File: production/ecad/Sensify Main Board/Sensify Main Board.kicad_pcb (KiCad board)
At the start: 4 copper layers, 150 parts, among them J1 1-2834011-3, J2 1-2834011-2, J3 1332645, J4 0532611271, J5 Screw_Terminal_01x08, J6 Conn_01x02_Socket, J7 Conn_01x02_Socket, J8 Conn_01x02_Socket, J9 Conn_01x02_Socket, Q1 2N700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

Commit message: continuing layout for main board
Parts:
- moved R1 220.4 mm to (210.3, 136.3), turned to -90 degrees
- moved R6 218.2 mm to (227.7, 118.3)
- moved R8 210.2 mm to (214.3, 128.5), turned to 180 degrees
- moved R9 209.9 mm to (217.3, 124.4), turned to 180 degrees
- moved R5 204.0 mm to (200.4, 124.4), turned to -90 degrees
- moved C7 200.9 mm to (214.9, 131.8), turned to 90 degrees
- moved R7 198.1 mm to (212.2, 112.5)
- moved BAT1+_TP1 125.7 mm to (112.1, 115.9)
- moved BAT1-/BAT2+_TP1 125.7 mm to (112.1, 119.5)
- moved BAT2-_TP1 125.7 mm to (112.1, 123.0)
- moved BMS_ALERT_TP1 125.7 mm to (112.1, 126.6)
- moved C16 125.7 mm to (96.6, 102.8)
- moved C17 125.7 mm to (101.9, 122.5)
- moved C18 125.7 mm to (96.6, 105.3)
- moved C20 125.7 mm to (96.6, 107.8)
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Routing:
- net (no net): vias 2 -> 0

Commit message: continued main board layout
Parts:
- U5: moved to B.Cu
- moved J3 247.1 mm to (246.7, 108.0)
- moved R31 227.2 mm to (253.1, 96.9), turned to -90 degrees
- moved R29 226.2 mm to (251.8, 96.9), turned to 90 degrees
- moved R28 225.0 mm to (250.6, 96.9), turned to 90 degrees
- moved R30 223.5 mm to (249.3, 96.9), turned to -90 degrees
- moved R25 181.6 mm to (207.8, 66.9)
- moved R32 181.6 mm to (210.7, 66.9)
- moved U6 179.4 mm to (196.6, 108.9)
- moved C24 176.2 mm to (213.2, 46.2)
- moved C25 176.2 mm to (213.2, 48.1)
- moved C26 176.2 mm to (213.2, 50.1)
- moved C27 176.2 mm to (213.2, 52.1)
- moved Q5 176.2 mm to (211.9, 32.4)
- moved Q6 176.2 mm to (211.9, 37.1)
- moved R26 176.2 mm to (200.4, 48.2)
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
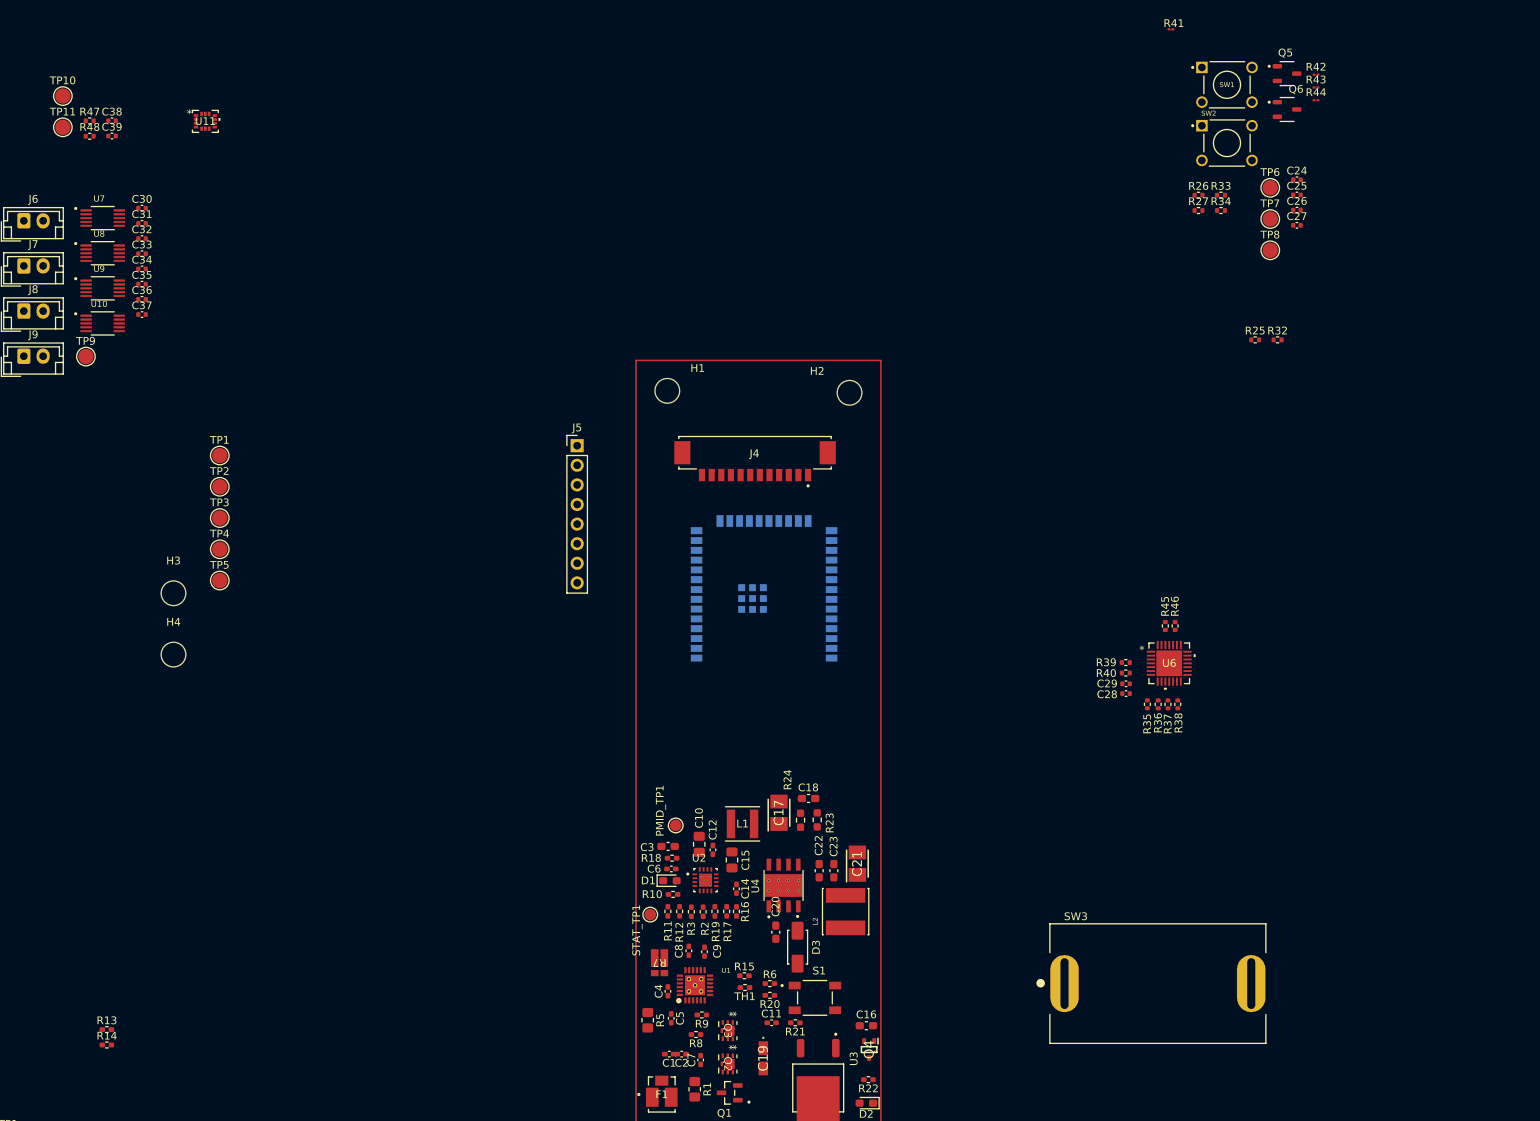
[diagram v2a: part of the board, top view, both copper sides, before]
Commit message: main board layout
rerouted the 5V buck supply according to TI guidelines
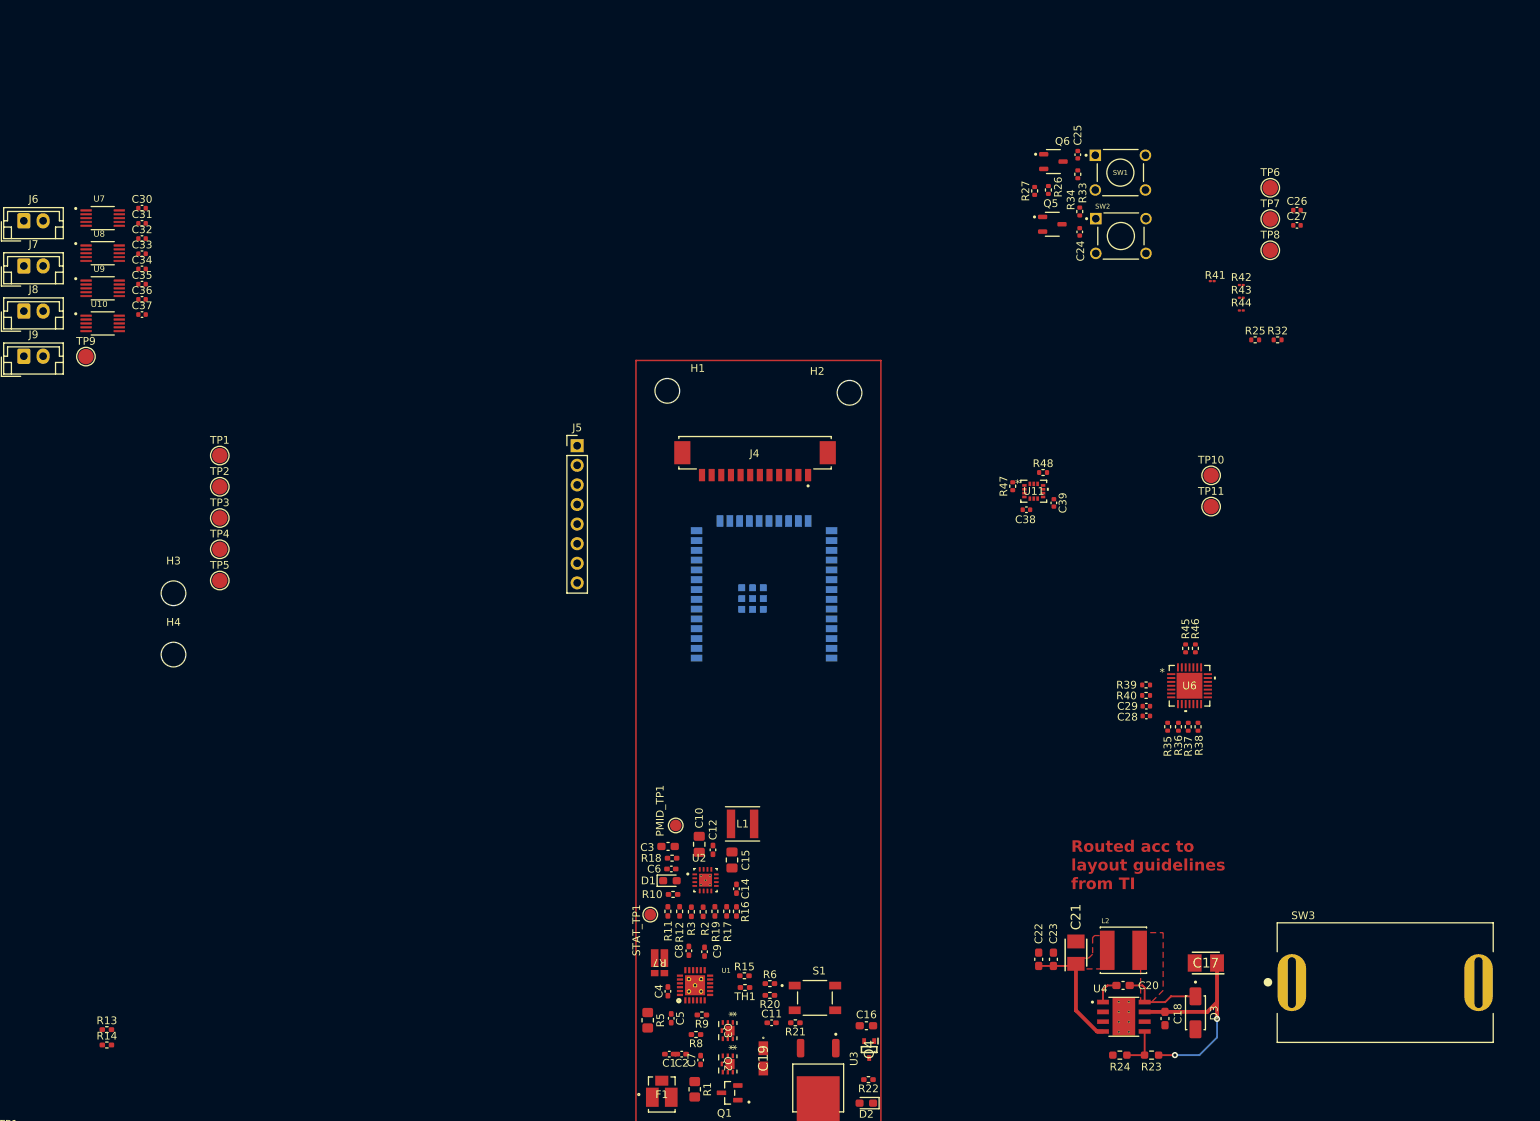
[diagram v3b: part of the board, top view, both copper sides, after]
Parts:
- moved TP10 156.7 mm to (202.1, 84.5)
- moved TP11 156.7 mm to (202.1, 88.5)
- moved R48 131.0 mm to (180.3, 84.1)
- moved C39 131.0 mm to (181.7, 88.1), turned to -90 degrees
- moved C38 128.8 mm to (178.1, 88.9)
- moved R47 128.7 mm to (176.3, 85.9), turned to 90 degrees
- moved U11 117.6 mm to (179.1, 86.5)
- moved C17 58.7 mm to (201.4, 147.7), turned to 180 degrees
- moved C18 54.3 mm to (196.1, 154.9), turned to -90 degrees
- moved R23 53.0 mm to (194.3, 159.6), turned to 180 degrees
- moved D3 52.3 mm to (200.0, 154.2)
- moved R24 51.4 mm to (190.2, 159.6), turned to 180 degrees
- moved U4 47.3 mm to (190.7, 154.7), turned to 0 degrees
- moved C20 45.5 mm to (190.6, 150.6), turned to 0 degrees
- moved L2 36.4 mm to (190.7, 146.1), turned to 180 degrees
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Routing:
- net Net-(SW3-B): track 0.00 -> 28.2 mm, vias 0 -> 2
- net +5V: track 0.00 -> 15.6 mm
- net Net-(U4-SW): track 0.00 -> 10.8 mm
- net Net-(U4-EN): track 0.00 -> 5.41 mm
- net Net-(U4-BOOT): track 0.00 -> 3.56 mm
- added copper zone on F.Cu, net +5V
- added copper zone on F.Cu, net Net-(U4-SW)
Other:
- board text added: "Routed acc to layout guidelines from TI"

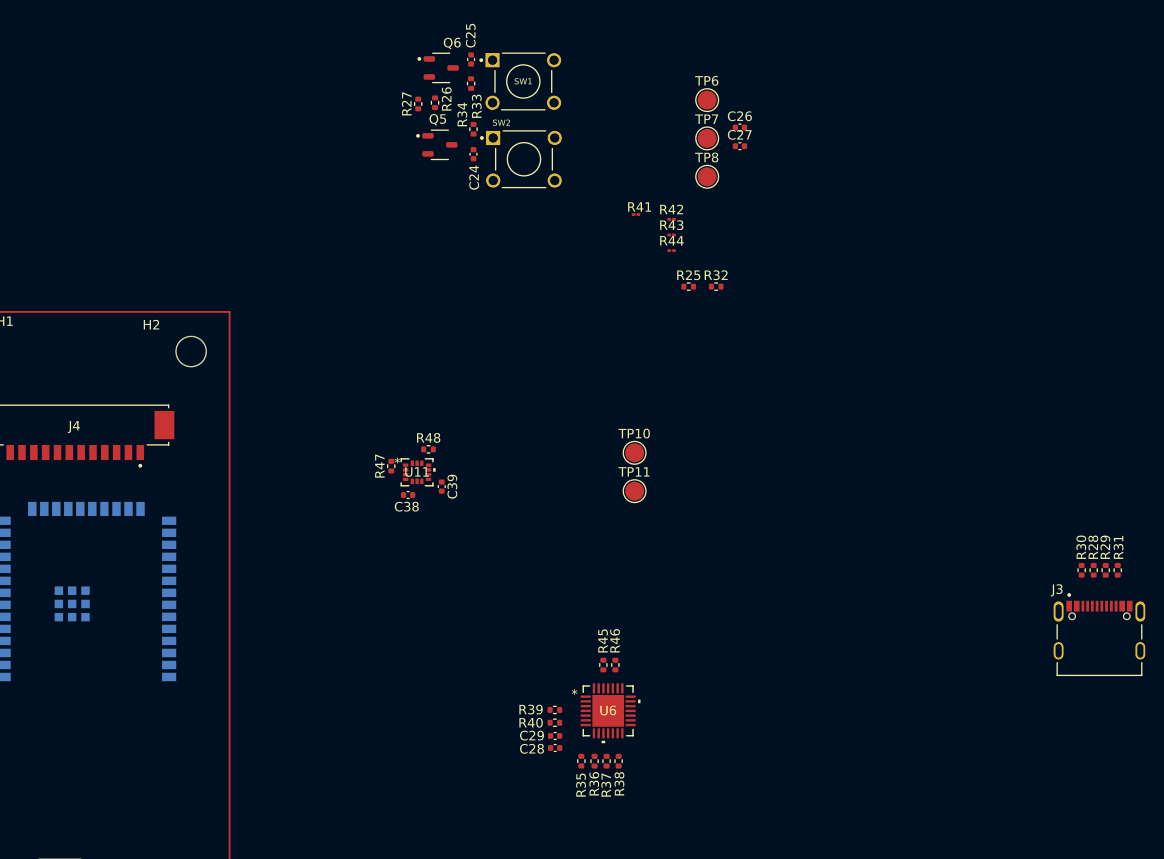
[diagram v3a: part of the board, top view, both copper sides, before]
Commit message: Routed most of USB-UART
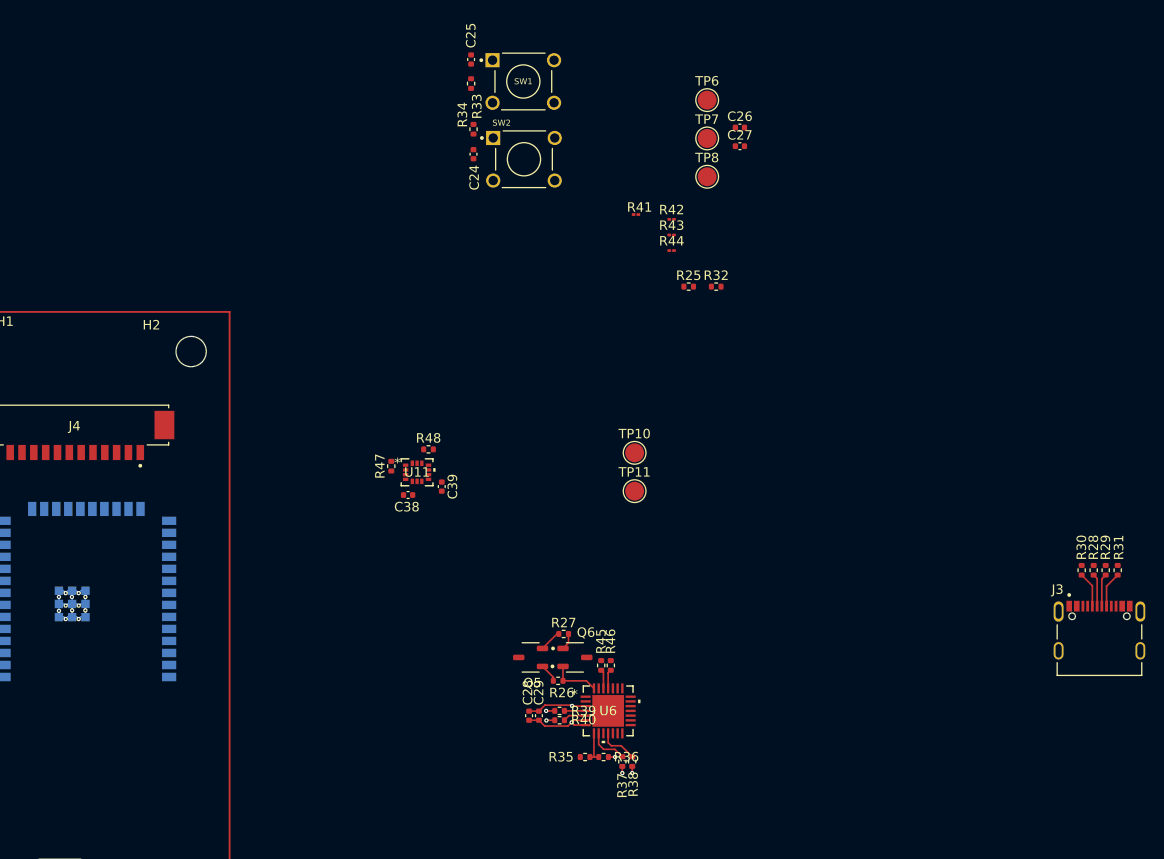
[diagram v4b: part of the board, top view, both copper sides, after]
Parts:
- moved Q6 63.9 mm to (195.7, 106.1)
- moved R26 62.5 mm to (194.0, 108.6), turned to 180 degrees
- moved R27 58.1 mm to (194.6, 103.6), turned to 0 degrees
- moved Q5 55.0 mm to (191.1, 106.1), turned to 180 degrees
- moved C28 4.39 mm to (190.9, 112.3), turned to 90 degrees
- moved C29 2.75 mm to (191.9, 112.3), turned to 90 degrees
- moved R37 1.66 mm to (200.8, 117.1)
- moved R38 1.44 mm to (201.8, 117.1)
- moved R36 1.05 mm to (198.8, 116.6), turned to 0 degrees
- moved R35 0.59 mm to (196.8, 116.6), turned to 0 degrees
- moved R40 0.56 mm to (194.1, 112.8), turned to 180 degrees
- moved R39 0.51 mm to (194.1, 111.8), turned to 180 degrees
- moved R46 0.48 mm to (199.5, 107.0)
- moved R45 0.23 mm to (198.5, 107.0)
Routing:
- net GND: track 0.00 -> 25.7 mm, vias 0 -> 15
- net +3V3: track 0.00 -> 8.80 mm, vias 0 -> 2
- net DTR: track 0.00 -> 5.13 mm
- net Net-(U6-RSTb): track 0.00 -> 4.21 mm
- net Net-(U6-SUSPENDb): track 0.00 -> 4.14 mm
- net Net-(J3-DP2): track 0.00 -> 3.77 mm
- net Net-(J3-DN2): track 0.00 -> 3.75 mm
- net Net-(J3-DN1): track 0.00 -> 3.45 mm
- net Net-(U6-VBUS): track 0.00 -> 3.45 mm
- net Net-(J3-DP1): track 0.00 -> 3.43 mm
- net Net-(U6-D-): track 0.00 -> 2.45 mm
- net RTS: track 0.00 -> 2.36 mm
- net Net-(U6-D+): track 0.00 -> 2.25 mm
- net Net-(U6-TXD): track 0.00 -> 2.17 mm
- net Net-(U6-RXD): track 0.00 -> 2.03 mm
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
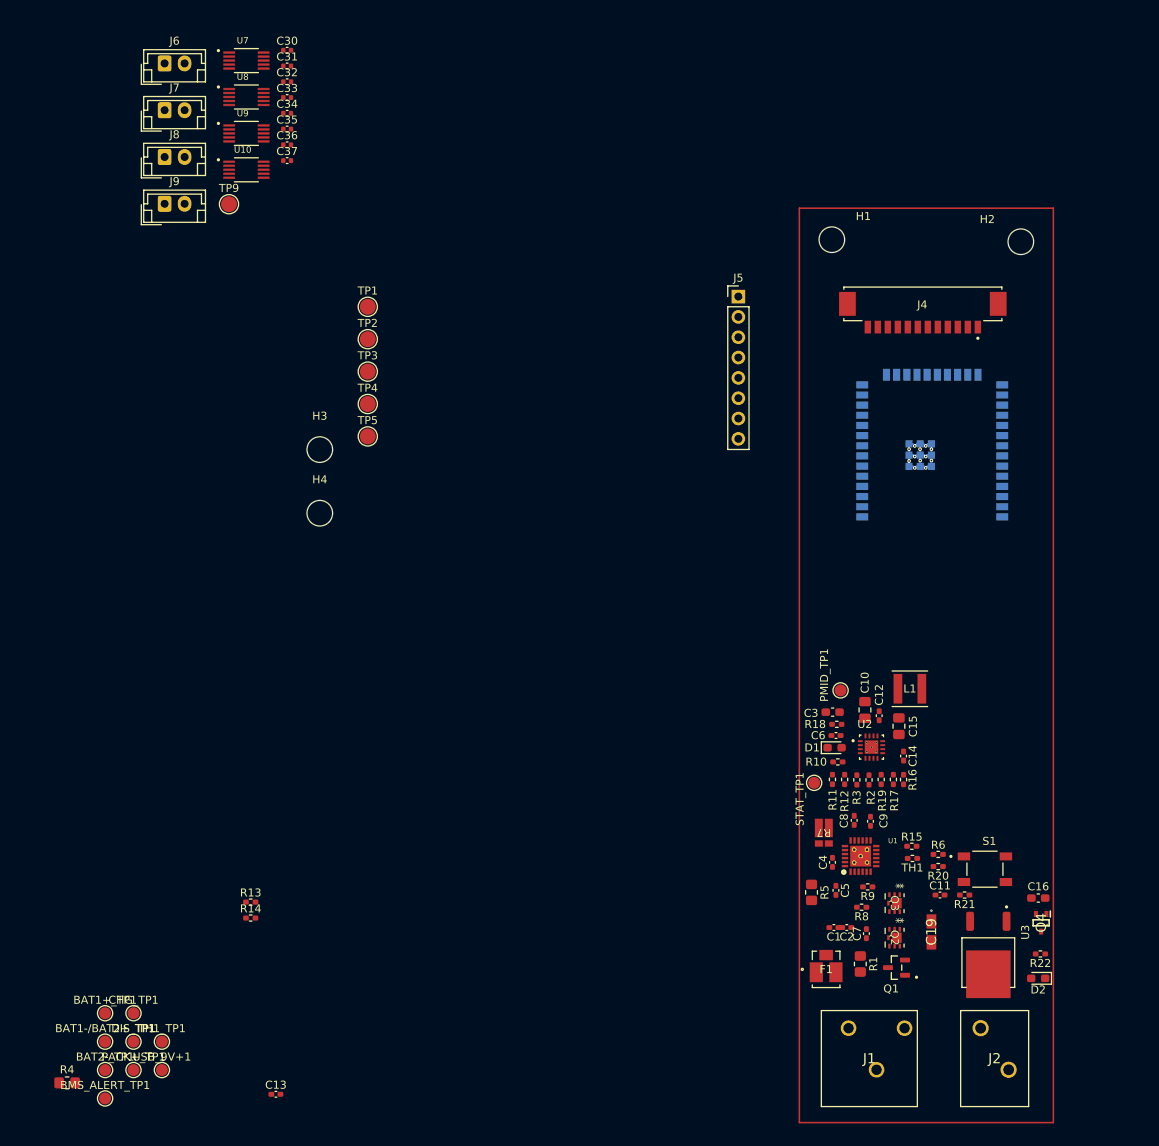
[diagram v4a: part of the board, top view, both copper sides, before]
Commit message: placed BMS components minus TPs
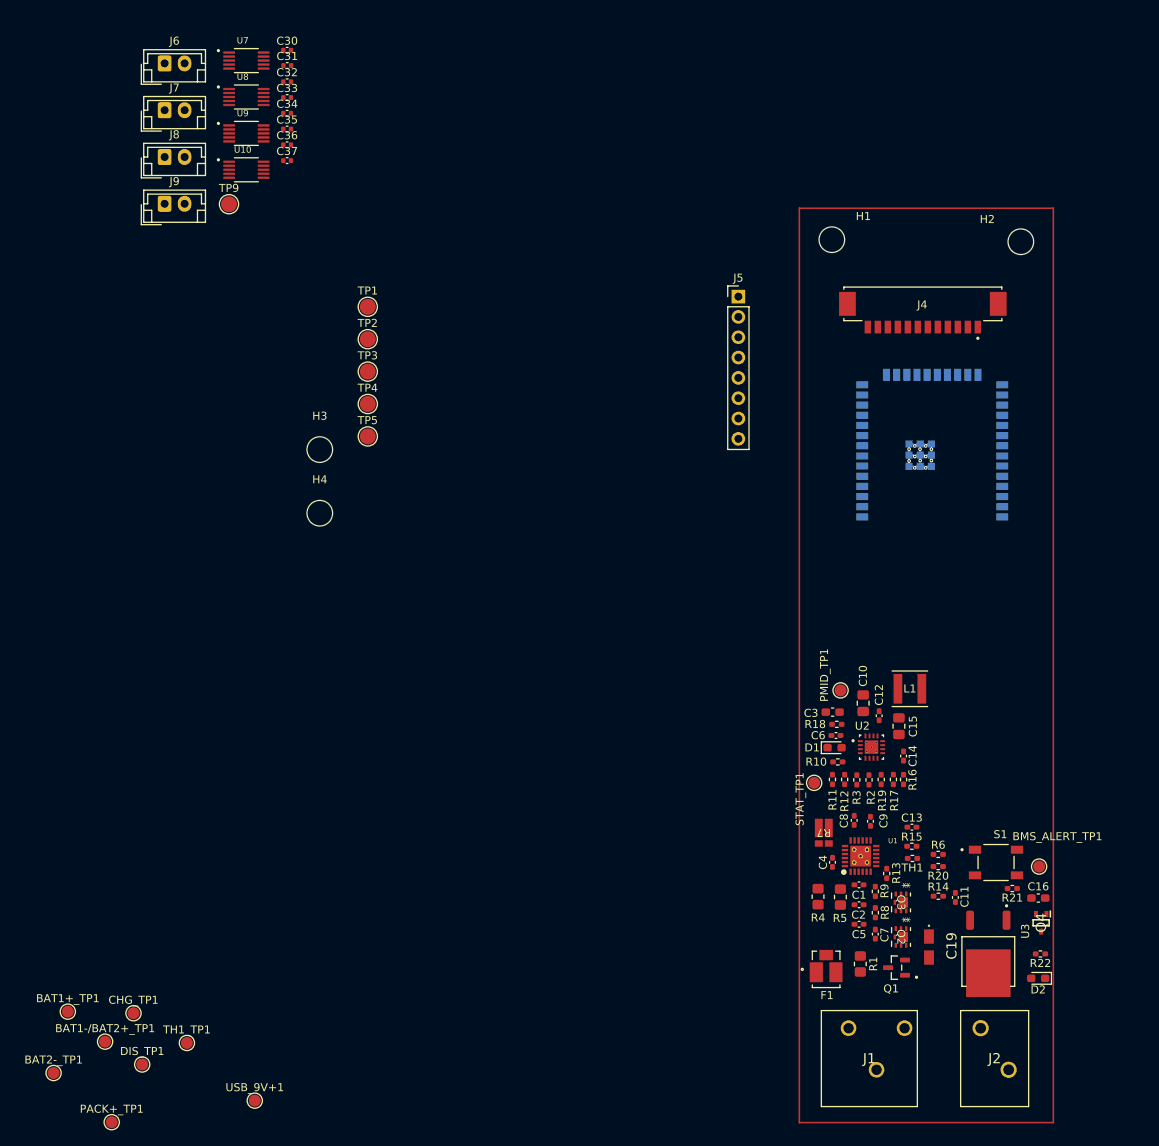
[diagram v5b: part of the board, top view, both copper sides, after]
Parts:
- moved BMS_ALERT_TP1 120.3 mm to (157.5, 151.9)
- moved R4 96.7 mm to (129.8, 155.7), turned to 90 degrees
- moved C13 86.2 mm to (141.6, 147.0)
- moved R14 86.0 mm to (144.9, 155.6)
- moved R13 79.6 mm to (138.4, 152.8), turned to 90 degrees
- moved USB_9V+1 12.2 mm to (59.4, 181.2)
- moved PACK+_TP1 7.07 mm to (41.6, 183.8)
- moved BAT2-_TP1 6.45 mm to (34.3, 177.7)
- moved C1 6.19 mm to (135.0, 154.2)
- moved R21 6.01 mm to (154.1, 154.6)
- moved C5 5.14 mm to (135.0, 159.1), turned to 0 degrees
- moved BAT1+_TP1 4.66 mm to (36.1, 170.0)
- moved R5 3.65 mm to (132.6, 155.7)
- moved C2 3.23 mm to (135.0, 156.7), turned to 0 degrees
- moved TH1_TP1 3.13 mm to (51.0, 173.9)
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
